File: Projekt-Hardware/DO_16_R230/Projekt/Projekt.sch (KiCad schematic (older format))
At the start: 44 parts, among them J1 COM_Bus, J2 COM_Bus, J3 ISP, J4 Conn_01x02, J5 Conn_01x08, J6 Conn_01x08, K1 DIPxx-1Cxx-51x, K10 DIPxx-1Cxx-51x, K11 DIPxx-1Cxx-51x, K12 DIPxx-1Cxx-51x, K13 DIPxx-1Cxx-51x, K14 DIPxx-1Cxx-51x, K15 DIPxx-1Cxx-51x, K16 DIPxx-1Cxx-51x, K2 DIPxx-1Cxx-51x, K3 DIPxx-1Cxx-51x, K4 DIPxx-1Cxx-51x, K5 DIPxx-1Cxx-51x, K6 DIPxx-1Cxx-51x, K7 DIPxx-1Cxx-51x, K8 DIPxx-1Cxx-51x, K9 DIPxx-1Cxx-51x, SW1 RESET, U1 ATmega328P-PU

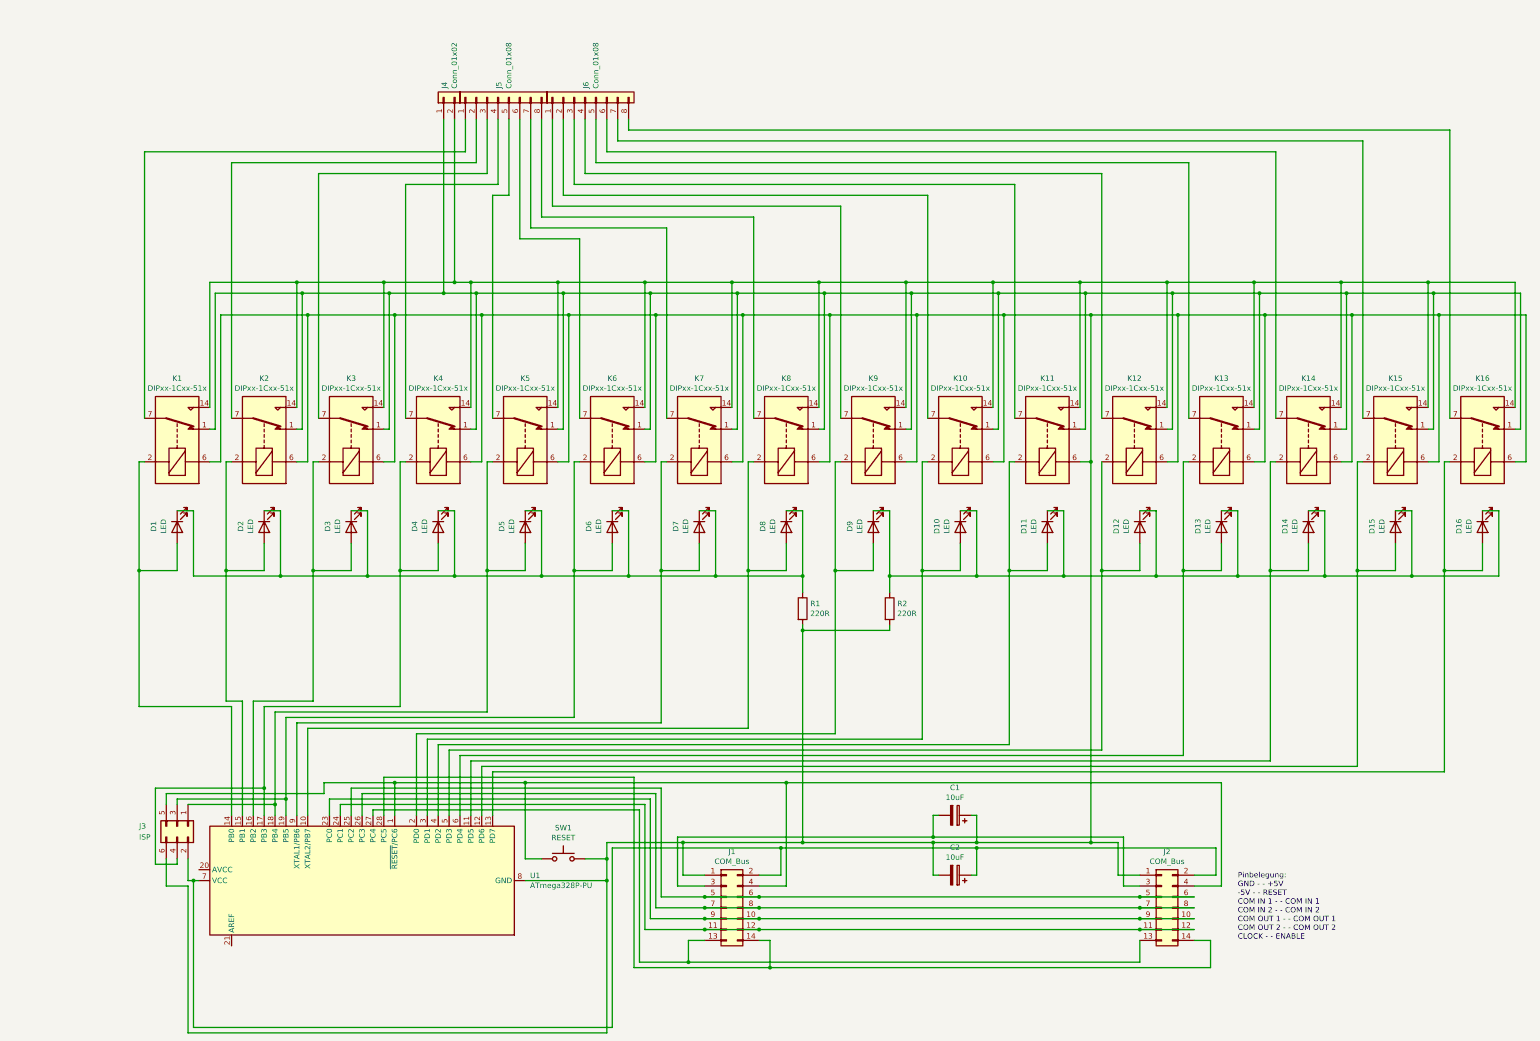
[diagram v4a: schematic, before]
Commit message: Hardware CNC Codes erstellt
Fertigungsdateien für eine CNC Version der
Leiterplatten erstellt.
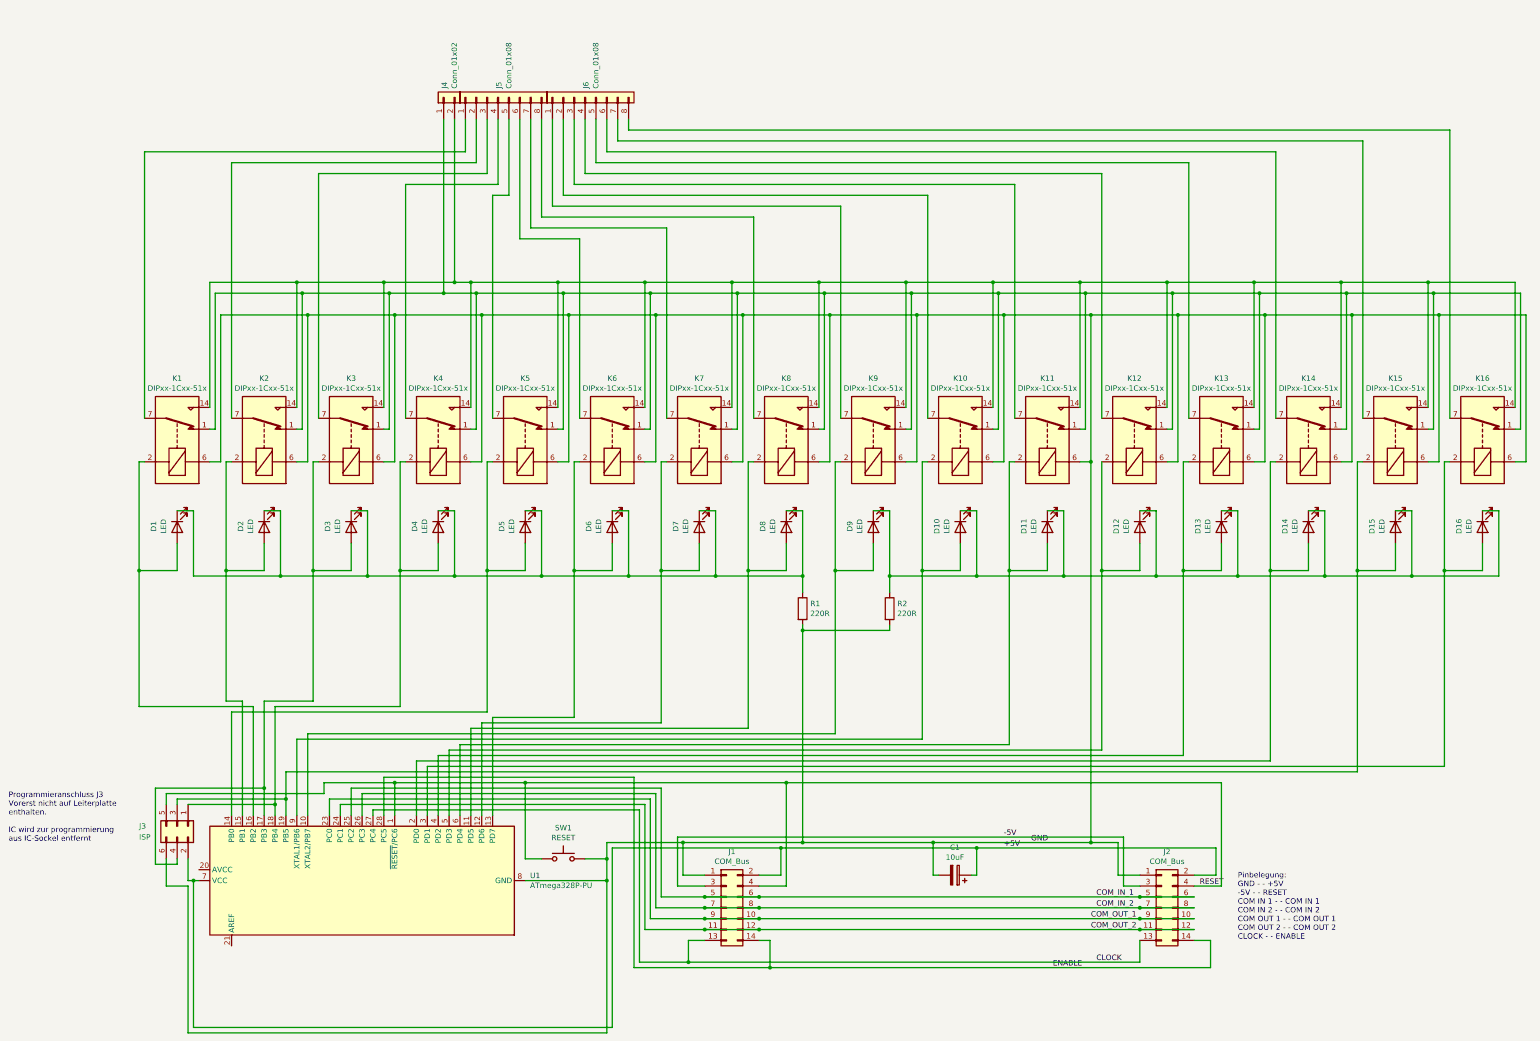
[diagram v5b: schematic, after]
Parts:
- removed C1: 10uF, Capacitor_THT:CP_Radial_D6.3mm_P2.50mm, symbol Device:CP
- renumbered C2 to C1
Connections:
- net at D7.2 (A), K7.2: now also U1.12 (PD6); no longer U1.9 (XTAL1/PB6)
- net GND: now reaches C1.2, J1.1 (Pin_1), J2.1 (Pin_1), J3.6 (Pin_6), K1.6, K10.6, K11.6, K12.6, K13.6, K14.6, K15.6, K16.6, K2.6, K3.6, K4.6, K5.6, K6.6, K7.6, K8.6, K9.6, R1.2, R2.2, SW1.2, U1.22 (GND), U1.8 (GND)
- net at D6.2 (A), K6.2: now also U1.13 (PD7); no longer J3.3 (Pin_3), U1.19 (PB5)
- net at D9.2 (A), K9.2: now also U1.10 (XTAL2/PB7); no longer U1.2 (PD0)
- net at D8.2 (A), K8.2: now also U1.11 (PD5); no longer U1.10 (XTAL2/PB7)
- net at D5.2 (A), K5.2: now also U1.14 (PB0); no longer J3.1 (Pin_1), U1.18 (PB4)
- net at D4.2 (A), K4.2: now also J3.1 (Pin_1), U1.18 (PB4); no longer J3.4 (Pin_4), U1.17 (PB3)
- net at D10.2 (A), K10.2: now also U1.9 (XTAL1/PB6); no longer U1.3 (PD1)
- net at D11.2 (A), K11.2: now also U1.6 (PD4); no longer U1.4 (PD2)
- net at D3.2 (A), K3.2: now also J3.4 (Pin_4), U1.17 (PB3); no longer U1.16 (PB2)
- net at D1.2 (A), K1.2: now also U1.16 (PB2); no longer U1.14 (PB0)
- net RESET: now reaches J1.4 (Pin_4), J2.4 (Pin_4), J3.5 (Pin_5), SW1.1, U1.1 (~RESET~/PC6)
- net at D14.2 (A), K14.2: now also U1.2 (PD0); no longer U1.11 (PD5)
- net at D15.2 (A), K15.2: now also J3.3 (Pin_3), U1.19 (PB5); no longer U1.12 (PD6)
- net at D16.2 (A), K16.2: now also U1.3 (PD1); no longer U1.13 (PD7)
- net COM_OUT_1: now reaches J1.10 (Pin_10), J1.9 (Pin_9), J2.10 (Pin_10), J2.9 (Pin_9), U1.23 (PC0)
- net COM_OUT_2: now reaches J1.11 (Pin_11), J1.12 (Pin_12), J2.11 (Pin_11), J2.12 (Pin_12), U1.24 (PC1)
- net COM_IN_1: now reaches J1.5 (Pin_5), J1.6 (Pin_6), J2.5 (Pin_5), J2.6 (Pin_6), U1.25 (PC2)
- net COM_IN_2: now reaches J1.7 (Pin_7), J1.8 (Pin_8), J2.7 (Pin_7), J2.8 (Pin_8), U1.26 (PC3)
- net CLOCK: now reaches J1.13 (Pin_13), J2.13 (Pin_13), U1.27 (PC4)
- net ENABLE: now reaches J1.14 (Pin_14), J2.14 (Pin_14), U1.28 (PC5)
- net at D13.2 (A), K13.2: now also U1.4 (PD2); no longer U1.6 (PD4)
- net +5V: now reaches C1.1, J1.2 (Pin_2), J2.2 (Pin_2), J3.2 (Pin_2), U1.7 (VCC)
- net -5V: now reaches J1.3 (Pin_3), J2.3 (Pin_3)
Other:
- note added: "Programmieranschluss J3\nVorerst nicht auf Leiterplatte\nenthalten.\n\nIC wird zur programmierung\naus IC-Sockel entfernt"
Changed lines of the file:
@@
 	11850 7350 11850 5650
 Wire Wire Line
-	13450 7450 13450 5650
-Wire Wire Line
-	14250 5650 14250 7500
+	14250 5650 14250 7450
 Wire Wire Line
 	2250 5650 2250 6900
@@
 Wire Wire Line
 	13800 5400 13800 5650
-Connection ~ 13450 5650
 Wire Wire Line
 	13450 4650 13450 5650
@@
 Pinbelegung:\nGND - - +5V\n-5V - - RESET\nCOM IN 1 - - COM IN 1\nCOM IN 2 - - COM IN 2\nCOM OUT 1 - - COM OUT 1\nCOM OUT 2 - - COM OUT 2\nCLOCK - - ENABLE
 Wire Wire Line
-	3300 6850 3300 7900
-Wire Wire Line
-	14250 7500 5500 7500
-Wire Wire Line
-	5500 7500 5500 7900
-Wire Wire Line
-	5400 7900 5400 7450
-Wire Wire Line
-	5400 7450 13450 7450
-Wire Wire Line
-	12650 7400 5300 7400
-Wire Wire Line
-	5300 7400 5300 7900
-Wire Wire Line
-	5200 7900 5200 7350
-Wire Wire Line
-	5200 7350 11850 7350
-Wire Wire Line
-	11100 7300 5100 7300
-Wire Wire Line
-	5100 7300 5100 7900
-Wire Wire Line
-	5000 7900 5000 7250
-Wire Wire Line
-	5000 7250 10250 7250
-Wire Wire Line
-	9450 7200 4900 7200
-Wire Wire Line
-	4900 7200 4900 7900
-Wire Wire Line
-	8650 7150 4800 7150
-Wire Wire Line
-	4800 7150 4800 7900
-Wire Wire Line
-	7850 7100 3800 7100
-Wire Wire Line
-	3800 7100 3800 7900
-Wire Wire Line
-	7050 7050 3700 7050
-Wire Wire Line
-	3700 7050 3700 7900
-Wire Wire Line
-	6250 7000 3600 7000
-Wire Wire Line
-	3600 7000 3600 7750
-Wire Wire Line
-	5450 6950 3500 6950
-Wire Wire Line
-	3500 6950 3500 7800
-Wire Wire Line
 	5450 5650 5450 6950
-Wire Wire Line
-	4650 6900 3400 6900
-Wire Wire Line
-	3850 6850 3300 6850
-Wire Wire Line
-	3200 6850 3050 6850
-Wire Wire Line
-	3100 6900 2250 6900
-Wire Wire Line
-	3100 6900 3100 7900
-Wire Wire Line
-	3200 6850 3200 7900
 Wire Wire Line
 	4600 7600 5800 7600
@@
 Wire Wire Line
 	3500 7800 2700 7800
-Connection ~ 3500 7800
 Wire Wire Line
 	3500 7800 3500 7900
 Wire Wire Line
 	2600 7750 3600 7750
-Connection ~ 3600 7750
 Wire Wire Line
 	3600 7750 3600 7900
@@
 Connection ~ 6550 8500
 Wire Wire Line
-	3400 6900 3400 7650
-Wire Wire Line
 	3400 7650 2400 7650
 Wire Wire Line
@@
 Wire Wire Line
 	2600 8350 2600 8300
-Connection ~ 3400 7650
 Wire Wire Line
 	3400 7650 3400 7900
@@
 Wire Wire Line
 	8150 8200 9950 8200
-Wire Wire Line
-	7200 8100 9550 8100
 Connection ~ 11450 8650
 Connection ~ 7950 8650
@@
 $Comp
 L Device:CP C1
-U 1 1 60095F7F
-P 9750 7900
-F 0 "C1" V 10005 7900 50  0000 C CNN
-F 1 "10uF" V 9914 7900 50  0000 C CNN
-F 2 "Capacitor_THT:CP_Radial_D6.3mm_P2.50mm" H 9788 7750 50  0001 C CNN
-F 3 "~" H 9750 7900 50  0001 C CNN
-	1    9750 7900
-	0    1    -1   0
-$EndComp
-$Comp
-L Device:CP C2
 U 1 1 600D41B0
 P 9750 8450
-F 0 "C2" V 10005 8450 50  0000 C CNN
+F 0 "C1" V 10005 8450 50  0000 C CNN
 F 1 "10uF" V 9914 8450 50  0000 C CNN
 F 2 "Capacitor_THT:CP_Radial_D6.3mm_P2.50mm" H 9788 8300 50  0001 C CNN
@@
 	9550 8450 9550 8150
 Connection ~ 9550 8150
-Wire Wire Line
-	9550 8150 9950 8150
-Wire Wire Line
-	9900 7900 9950 7900
-Wire Wire Line
-	9950 7900 9950 8150
-Connection ~ 9950 8150
-Wire Wire Line
-	9950 8150 11000 8150
-Wire Wire Line
-	9550 7900 9550 8100
-Connection ~ 9550 8100
-Wire Wire Line
-	9550 8100 11300 8100
-Wire Wire Line
-	9550 7900 9600 7900
+Text Label 10200 8100 0    50   ~ 0
+-5V
+Text Label 10200 8200 0    50   ~ 0
++5V
+Text Label 10450 8150 0    50   ~ 0
+GND
+Wire Wire Line
+	9550 8150 11000 8150
+Wire Wire Line
+	7200 8100 11300 8100
+Text Label 11050 9250 0    50   ~ 0
+CLOCK
+Text Label 10650 9300 0    50   ~ 0
+ENABLE
+Text Label 11050 8650 0    50   ~ 0
+COM_IN_1
+Text Label 11050 8750 0    50   ~ 0
+COM_IN_2
+Text Label 11000 8850 0    50   ~ 0
+COM_OUT_1
+Text Label 11000 8950 0    50   ~ 0
+COM_OUT_2
+Wire Wire Line
+	3300 6900 3300 7900
+Wire Wire Line
+	2250 6900 3300 6900
+Wire Wire Line
+	3400 7650 3400 6850
+Connection ~ 3400 7650
+Wire Wire Line
+	3400 6850 3850 6850
+Wire Wire Line
+	4650 6900 3500 6900
+Connection ~ 3500 7800
+Wire Wire Line
+	3500 6900 3500 7800
+Wire Wire Line
+	5450 6950 3100 6950
+Wire Wire Line
+	3100 6950 3100 7900
+Wire Wire Line
+	13450 5650 13450 7500
+Connection ~ 13450 5650
+Wire Wire Line
+	3050 6850 3200 6850
+Wire Wire Line
+	3200 6850 3200 7900
+Wire Wire Line
+	7850 7100 5300 7100
+Wire Wire Line
+	5300 7100 5300 7900
+Wire Wire Line
+	8650 7150 3800 7150
+Wire Wire Line
+	3800 7150 3800 7900
+Wire Wire Line
+	9450 7200 3700 7200
+Wire Wire Line
+	3700 7200 3700 7900
+Wire Wire Line
+	10250 7250 5200 7250
+Wire Wire Line
+	5400 7050 5400 7900
+Wire Wire Line
+	5500 7000 6250 7000
+Wire Wire Line
+	5500 7000 5500 7900
+Wire Wire Line
+	5400 7050 7050 7050
+Wire Wire Line
+	5200 7250 5200 7900
+Wire Wire Line
+	5100 7300 11100 7300
+Wire Wire Line
+	5100 7300 5100 7900
+Wire Wire Line
+	11850 7350 5000 7350
+Wire Wire Line
+	5000 7350 5000 7900
+Wire Wire Line
+	12650 7400 4800 7400
+Wire Wire Line
+	4800 7400 4800 7900
+Wire Wire Line
+	14250 7450 4900 7450
+Wire Wire Line
+	4900 7450 4900 7900
+Wire Wire Line
+	3600 7750 3600 7500
+Wire Wire Line
+	3600 7500 13450 7500
+Connection ~ 3600 7750
+Text Label 12000 8550 0    50   ~ 0
+RESET
+Text Notes 1050 8150 0    50   ~ 0
+Programmieranschluss J3\nVorerst nicht auf Leiterplatte\nenthalten.\n\nIC wird zur programmierung\naus IC-Sockel entfernt
 $EndSCHEMATC
